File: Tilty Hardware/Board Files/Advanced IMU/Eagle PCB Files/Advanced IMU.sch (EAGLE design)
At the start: 13 parts, among them U3 MPL3115A2LGA8, U6 HMC5883LSMD

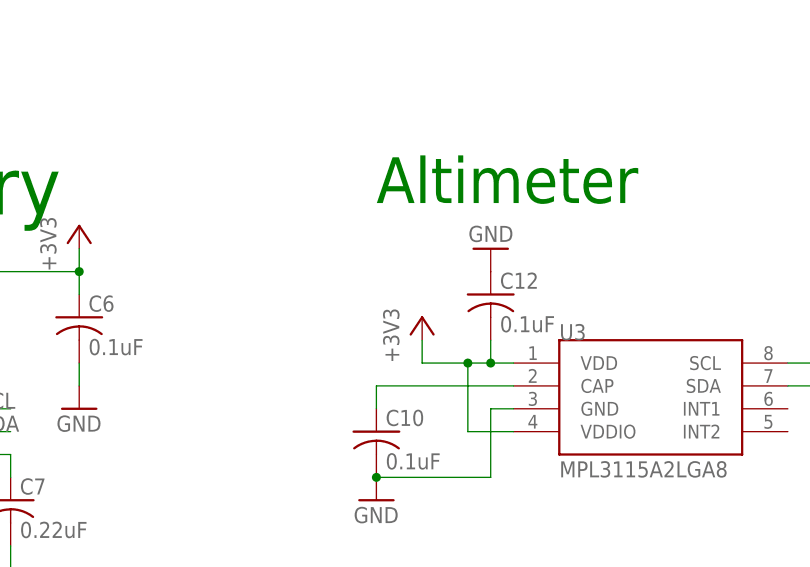
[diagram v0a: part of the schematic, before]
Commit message: Minor changes
Added current limit resistor to zener shunt on Tilty Duo/Quad.
Added power supply solder jumper to Advanced IMU altimeter.
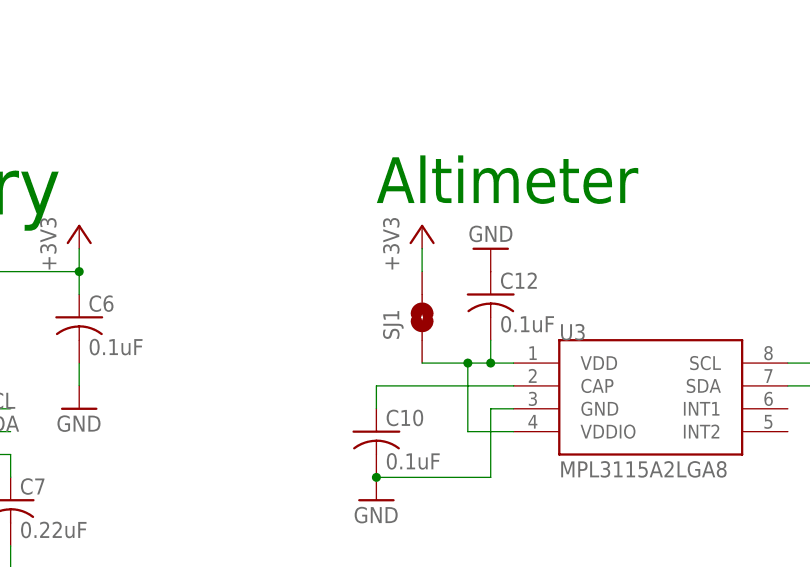
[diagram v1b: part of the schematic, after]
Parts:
- added SJ1: SOLDERJUMPERNC, SparkFun-Passives:SOLDERJUMPERNC
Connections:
- new net N$3: C12.2, SJ1.1, U3.VDD, U3.VDDIO
- net +3V3: now also SJ1.2; no longer C12.2, U3.VDD, U3.VDDIO
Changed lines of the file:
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@@
 <part name="+3V4" library="supply1" deviceset="+3V3" device=""/>
 <part name="GND1" library="SparkFun" deviceset="GND" device=""/>
+<part name="SJ1" library="SparkFun-Passives" deviceset="SOLDERJUMPER" device="NC"/>
 </parts>
 <sheets>
@@
 <instance part="GND25" gate="1" x="187.96" y="91.44" rot="R180"/>
 <instance part="+3V2" gate="G$1" x="142.24" y="93.98"/>
-<instance part="+3V3" gate="G$1" x="180.34" y="83.82"/>
+<instance part="+3V3" gate="G$1" x="180.34" y="93.98"/>
 <instance part="JP5" gate="G$1" x="73.66" y="25.4" rot="MR180"/>
 <instance part="JP6" gate="G$1" x="101.6" y="25.4" rot="R180"/>
 <instance part="+3V4" gate="G$1" x="88.9" y="35.56"/>
 <instance part="GND1" gate="1" x="86.36" y="15.24"/>
+<instance part="SJ1" gate="1" x="180.34" y="83.82" smashed="yes" rot="R90">
+<attribute name="NAME" x="177.8" y="81.28" size="1.778" layer="95" rot="R90"/>
+</instance>
 </instances>
 <busses>
@@
 </segment>
 <segment>
+<pinref part="JP5" gate="G$1" pin="1"/>
+<pinref part="JP6" gate="G$1" pin="1"/>
+<wire x1="78.74" y1="27.94" x2="88.9" y2="27.94" width="0.1524" layer="91"/>
+<pinref part="+3V4" gate="G$1" pin="+3V3"/>
+<wire x1="88.9" y1="27.94" x2="96.52" y2="27.94" width="0.1524" layer="91"/>
+<wire x1="88.9" y1="27.94" x2="88.9" y2="33.02" width="0.1524" layer="91"/>
+<junction x="88.9" y="27.94"/>
+</segment>
+<segment>
+<pinref part="SJ1" gate="1" pin="2"/>
+<pinref part="+3V3" gate="G$1" pin="+3V3"/>
+<wire x1="180.34" y1="88.9" x2="180.34" y2="91.44" width="0.1524" layer="91"/>
+</segment>
+</net>
+<net name="+5V" class="0">
+<segment>
+<pinref part="JP4" gate="G$1" pin="1"/>
+<pinref part="P+1" gate="1" pin="+5V"/>
+<wire x1="5.08" y1="20.32" x2="25.4" y2="20.32" width="0.1524" layer="91"/>
+<wire x1="25.4" y1="20.32" x2="25.4" y2="25.4" width="0.1524" layer="91"/>
+</segment>
+</net>
+<net name="VCC" class="0">
+<segment>
+<pinref part="JP2" gate="G$1" pin="7"/>
+<wire x1="5.08" y1="60.96" x2="30.48" y2="60.96" width="0.1524" layer="91"/>
+<pinref part="P+2" gate="VCC" pin="VCC"/>
+<wire x1="30.48" y1="60.96" x2="30.48" y2="63.5" width="0.1524" layer="91"/>
+</segment>
+</net>
+<net name="N$1" class="0">
+<segment>
+<wire x1="124.46" y1="66.04" x2="127" y2="66.04" width="0.1524" layer="91"/>
+<wire x1="127" y1="66.04" x2="127" y2="68.58" width="0.1524" layer="91"/>
+<wire x1="127" y1="68.58" x2="134.62" y2="68.58" width="0.1524" layer="91"/>
+<wire x1="134.62" y1="68.58" x2="134.62" y2="66.04" width="0.1524" layer="91"/>
+<pinref part="U6" gate="G$1" pin="SETP"/>
+<pinref part="C7" gate="G$1" pin="1"/>
+</segment>
+</net>
+<net name="N$2" class="0">
+<segment>
+<wire x1="124.46" y1="63.5" x2="127" y2="63.5" width="0.1524" layer="91"/>
+<wire x1="127" y1="63.5" x2="127" y2="55.88" width="0.1524" layer="91"/>
+<wire x1="127" y1="55.88" x2="134.62" y2="55.88" width="0.1524" layer="91"/>
+<wire x1="134.62" y1="55.88" x2="134.62" y2="58.42" width="0.1524" layer="91"/>
+<pinref part="U6" gate="G$1" pin="SETC"/>
+<pinref part="C7" gate="G$1" pin="2"/>
+</segment>
+</net>
+<net name="N$11" class="0">
+<segment>
+<wire x1="81.28" y1="66.04" x2="81.28" y2="68.58" width="0.1524" layer="91"/>
+<wire x1="81.28" y1="68.58" x2="93.98" y2="68.58" width="0.1524" layer="91"/>
+<pinref part="U6" gate="G$1" pin="C1"/>
+<pinref part="C8" gate="G$1" pin="1"/>
+</segment>
+</net>
+<net name="N$21" class="0">
+<segment>
+<pinref part="U3" gate="G$1" pin="CAP"/>
+<pinref part="C10" gate="G$1" pin="1"/>
+<wire x1="190.5" y1="76.2" x2="175.26" y2="76.2" width="0.1524" layer="91"/>
+<wire x1="175.26" y1="76.2" x2="175.26" y2="73.66" width="0.1524" layer="91"/>
+</segment>
+</net>
+<net name="N$3" class="0">
+<segment>
 <pinref part="U3" gate="G$1" pin="VDD"/>
 <pinref part="U3" gate="G$1" pin="VDDIO"/>
@@
 <wire x1="187.96" y1="81.28" x2="187.96" y2="78.74" width="0.1524" layer="91"/>
 <junction x="187.96" y="78.74"/>
-<pinref part="+3V3" gate="G$1" pin="+3V3"/>
 <wire x1="185.42" y1="78.74" x2="180.34" y2="78.74" width="0.1524" layer="91"/>
-<wire x1="180.34" y1="78.74" x2="180.34" y2="81.28" width="0.1524" layer="91"/>
 <junction x="185.42" y="78.74"/>
-</segment>
-<segment>
-<pinref part="JP5" gate="G$1" pin="1"/>
-<pinref part="JP6" gate="G$1" pin="1"/>
-<wire x1="78.74" y1="27.94" x2="88.9" y2="27.94" width="0.1524" layer="91"/>
-<pinref part="+3V4" gate="G$1" pin="+3V3"/>
-<wire x1="88.9" y1="27.94" x2="96.52" y2="27.94" width="0.1524" layer="91"/>
-<wire x1="88.9" y1="27.94" x2="88.9" y2="33.02" width="0.1524" layer="91"/>
-<junction x="88.9" y="27.94"/>
-</segment>
-</net>
-<net name="+5V" class="0">
-<segment>
-<pinref part="JP4" gate="G$1" pin="1"/>
-<pinref part="P+1" gate="1" pin="+5V"/>
-<wire x1="5.08" y1="20.32" x2="25.4" y2="20.32" width="0.1524" layer="91"/>
-<wire x1="25.4" y1="20.32" x2="25.4" y2="25.4" width="0.1524" layer="91"/>
-</segment>
-</net>
-<net name="VCC" class="0">
-<segment>
-<pinref part="JP2" gate="G$1" pin="7"/>
-<wire x1="5.08" y1="60.96" x2="30.48" y2="60.96" width="0.1524" layer="91"/>
-<pinref part="P+2" gate="VCC" pin="VCC"/>
-<wire x1="30.48" y1="60.96" x2="30.48" y2="63.5" width="0.1524" layer="91"/>
-</segment>
-</net>
-<net name="N$1" class="0">
-<segment>
-<wire x1="124.46" y1="66.04" x2="127" y2="66.04" width="0.1524" layer="91"/>
-<wire x1="127" y1="66.04" x2="127" y2="68.58" width="0.1524" layer="91"/>
-<wire x1="127" y1="68.58" x2="134.62" y2="68.58" width="0.1524" layer="91"/>
-<wire x1="134.62" y1="68.58" x2="134.62" y2="66.04" width="0.1524" layer="91"/>
-<pinref part="U6" gate="G$1" pin="SETP"/>
-<pinref part="C7" gate="G$1" pin="1"/>
-</segment>
-</net>
-<net name="N$2" class="0">
-<segment>
-<wire x1="124.46" y1="63.5" x2="127" y2="63.5" width="0.1524" layer="91"/>
-<wire x1="127" y1="63.5" x2="127" y2="55.88" width="0.1524" layer="91"/>
-<wire x1="127" y1="55.88" x2="134.62" y2="55.88" width="0.1524" layer="91"/>
-<wire x1="134.62" y1="55.88" x2="134.62" y2="58.42" width="0.1524" layer="91"/>
-<pinref part="U6" gate="G$1" pin="SETC"/>
-<pinref part="C7" gate="G$1" pin="2"/>
-</segment>
-</net>
-<net name="N$11" class="0">
-<segment>
-<wire x1="81.28" y1="66.04" x2="81.28" y2="68.58" width="0.1524" layer="91"/>
-<wire x1="81.28" y1="68.58" x2="93.98" y2="68.58" width="0.1524" layer="91"/>
-<pinref part="U6" gate="G$1" pin="C1"/>
-<pinref part="C8" gate="G$1" pin="1"/>
-</segment>
-</net>
-<net name="N$21" class="0">
-<segment>
-<pinref part="U3" gate="G$1" pin="CAP"/>
-<pinref part="C10" gate="G$1" pin="1"/>
-<wire x1="190.5" y1="76.2" x2="175.26" y2="76.2" width="0.1524" layer="91"/>
-<wire x1="175.26" y1="76.2" x2="175.26" y2="73.66" width="0.1524" layer="91"/>
-</segment>
-</net>
+<pinref part="SJ1" gate="1" pin="1"/>
+</segment>
+</net>
